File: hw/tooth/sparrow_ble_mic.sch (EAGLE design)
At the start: 25 parts, among them Q2 FA-128

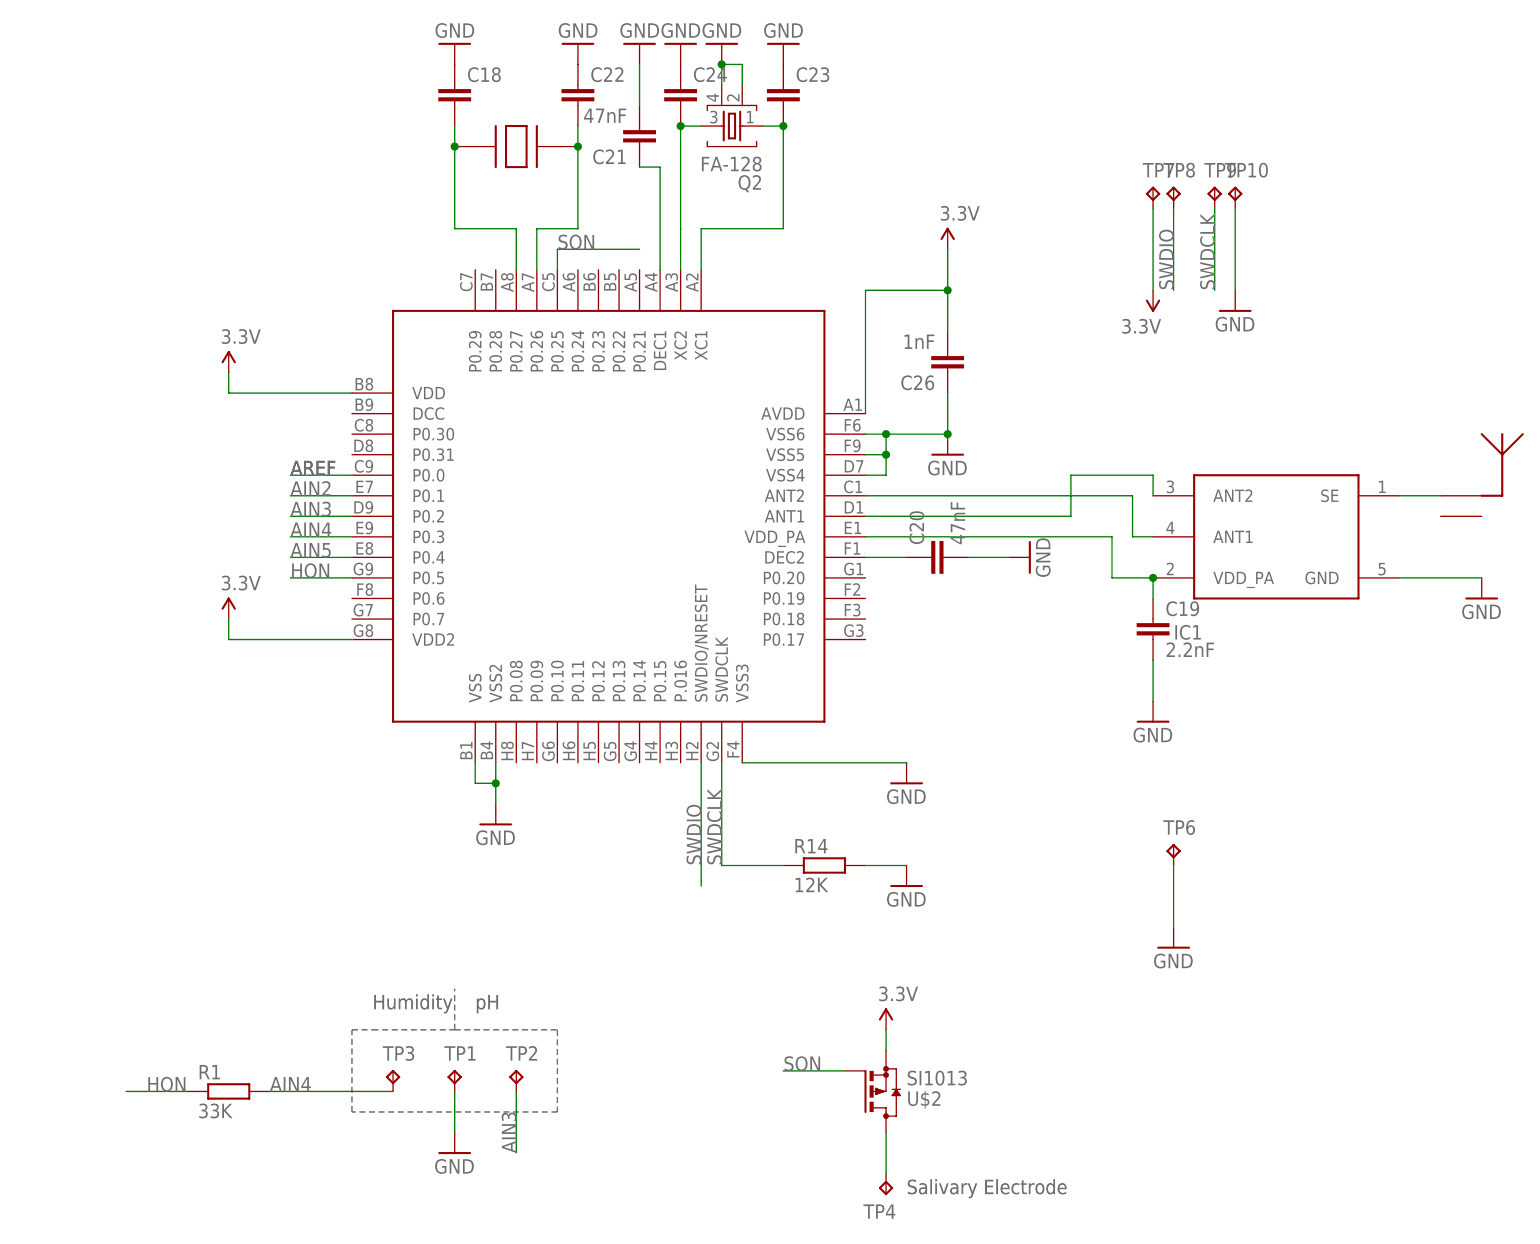
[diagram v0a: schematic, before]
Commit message: hw: Update tooth design for nRF52832
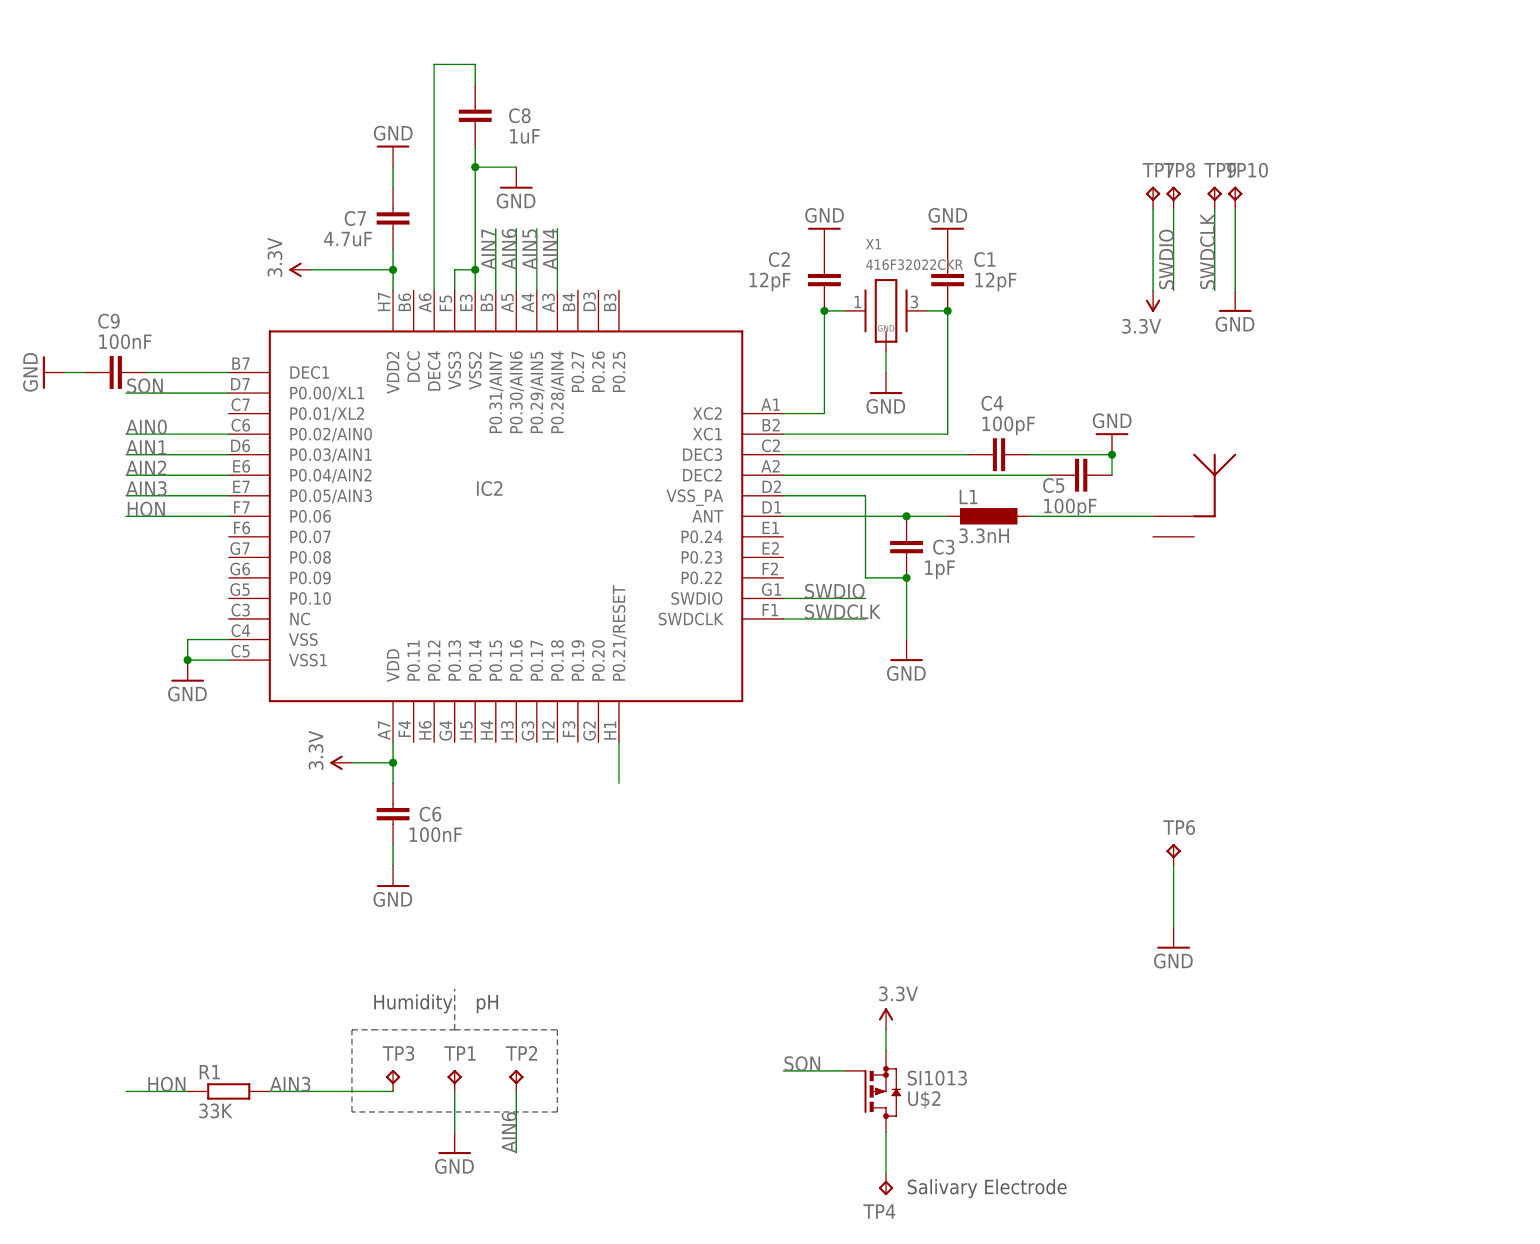
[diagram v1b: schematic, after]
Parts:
- removed C18, C22, C23, C24: (no value), rcl:C-EUC0201
- removed C19: 2.2nF, rcl:C-EUC0201
- removed C20, C21: 47nF, rcl:C-EUC0201
- removed C26: 1nF, rcl:C-EUC0201
- removed IC1: (no value), dan:2450BM08B0003T
- removed IC3: (no value), dan:NRF51822_WLCSP
- removed Q2: FA-128, smartwatch:FA-128
- removed R14: 12K, rcl:R-EU_R0201
- removed U$1: 2450AT18A100, dan:2450AT18A100
- removed U$4: ABS05, dan:ABS05
- added C1, C2: 12pF, rcl:C-EUC0201
- added C3: 1pF, rcl:C-EUC0201
- added C4, C5: 100pF, rcl:C-EUC0201
- added C6, C9: 100nF, rcl:C-EUC0201
- added C7: 4.7uF, rcl:C-EUC0402
- added C8: 1uF, rcl:C-EUC0402
- added IC2: (no value), dan:NRF52832
- added L1: 3.3nH, rcl:L-EUL0201
- added U$3: 2450AT18A100, dan:2450AT18A100
- added X1: 416F32022CKR, crystals:M416F26022CKR
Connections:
- removed net AREF: IC3.P0.0
- removed net N$11: C21.1, IC3.DEC1
- removed net N$15: C20.1, IC3.DEC2
- removed net N$16: C19.1, IC1.VDD_PA, IC3.VDD_PA
- removed net N$17: C24.2, IC3.XC2, Q2.3
- removed net N$18: C23.2, IC3.XC1, Q2.1
- removed net N$3: IC1.ANT2, IC3.ANT1
- removed net N$4: IC1.SE, U$1.P$1
- removed net N$7: C18.2, IC3.P0.27, U$4.P$1
- removed net N$8: C22.2, IC3.P0.26, U$4.P$2
- new net AIN0: IC2.P0.02/AIN0
- new net AIN1: IC2.P0.03/AIN1
- new net AIN6: IC2.P0.30/AIN6, TP2.TP
- new net AIN7: IC2.P0.31/AIN7
- new net N$10: C5.1, IC2.DEC2
- new net N$12: C3.1, IC2.ANT, L1.2
- new net N$13: L1.1, U$3.P$1
- new net N$19: C9.1, IC2.DEC1
- new net N$2: C2.2, IC2.XC2, X1.1
- new net N$20: C8.1, IC2.DEC4
- new net N$6: C1.2, IC2.XC1, X1.2
- new net N$9: C4.1, IC2.DEC3
- net 3.3V: now also C6.2, C7.2, IC2.VDD, IC2.VDD2; no longer C26.2, IC3.AVDD, IC3.VDD, IC3.VDD2
- net AIN2: now also IC2.P0.04/AIN2; no longer IC3.P0.1
- net AIN3: now also IC2.P0.05/AIN3, R1.2, TP3.TP; no longer IC3.P0.2, TP2.TP
- net AIN4: now also IC2.P0.28/AIN4; no longer IC3.P0.3, R1.2, TP3.TP
- net AIN5: now also IC2.P0.29/AIN5; no longer IC3.P0.4
- net GND: now also C1.1, C2.1, C3.2, C4.2, C5.2, C6.1, C7.1, C8.2, C9.2, IC2.VSS, IC2.VSS1, IC2.VSS2, IC2.VSS3, IC2.VSS_PA, X1.GND; no longer C18.1, C19.2, C20.2, C21.2, C22.1, C23.1, C24.1, C26.1, IC1.GND, IC3.VSS, IC3.VSS2, IC3.VSS3, IC3.VSS4, IC3.VSS5, IC3.VSS6, Q2.2, Q2.4, R14.2
- net HON: now also IC2.P0.06; no longer IC3.P0.5
- net N$1: now also IC2.P0.21/RESET; no longer IC1.ANT1, IC3.ANT2
- net SON: now also IC2.P0.00/XL1; no longer IC3.P0.25
- net SWDCLK: now also IC2.SWDCLK; no longer IC3.SWDCLK, R14.1
- net SWDIO: now also IC2.SWDIO; no longer IC3.SWDIO/NRESET
